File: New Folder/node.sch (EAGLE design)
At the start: 11 parts, among them IC1 TINY24/44/84-SSU

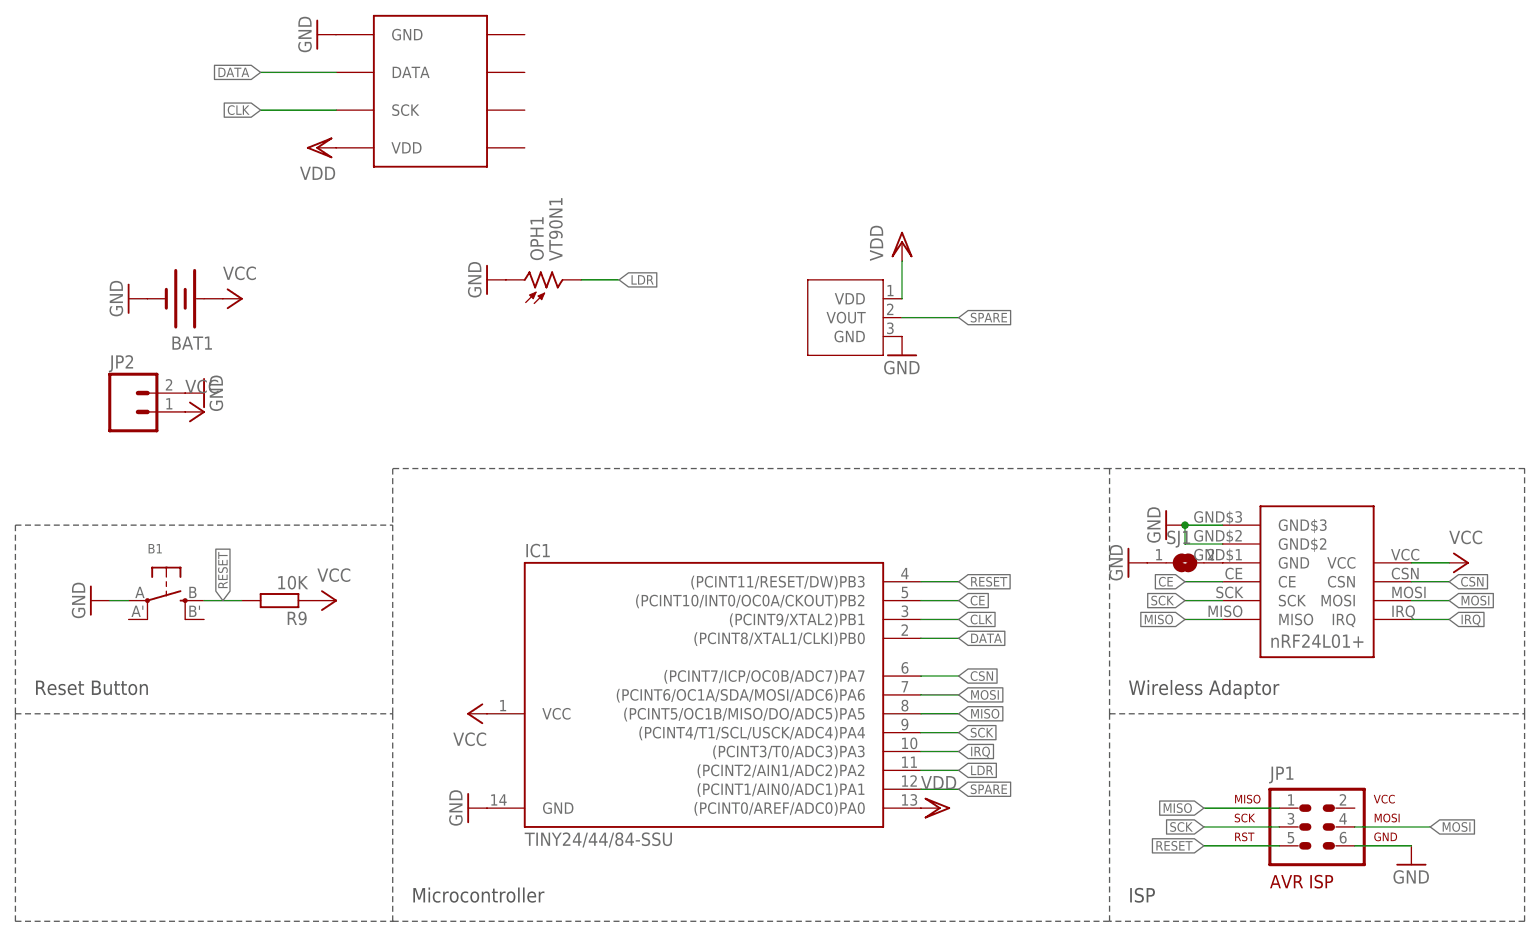
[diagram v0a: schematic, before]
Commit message: Added HA node v0.2, now with battery voltage monitoring
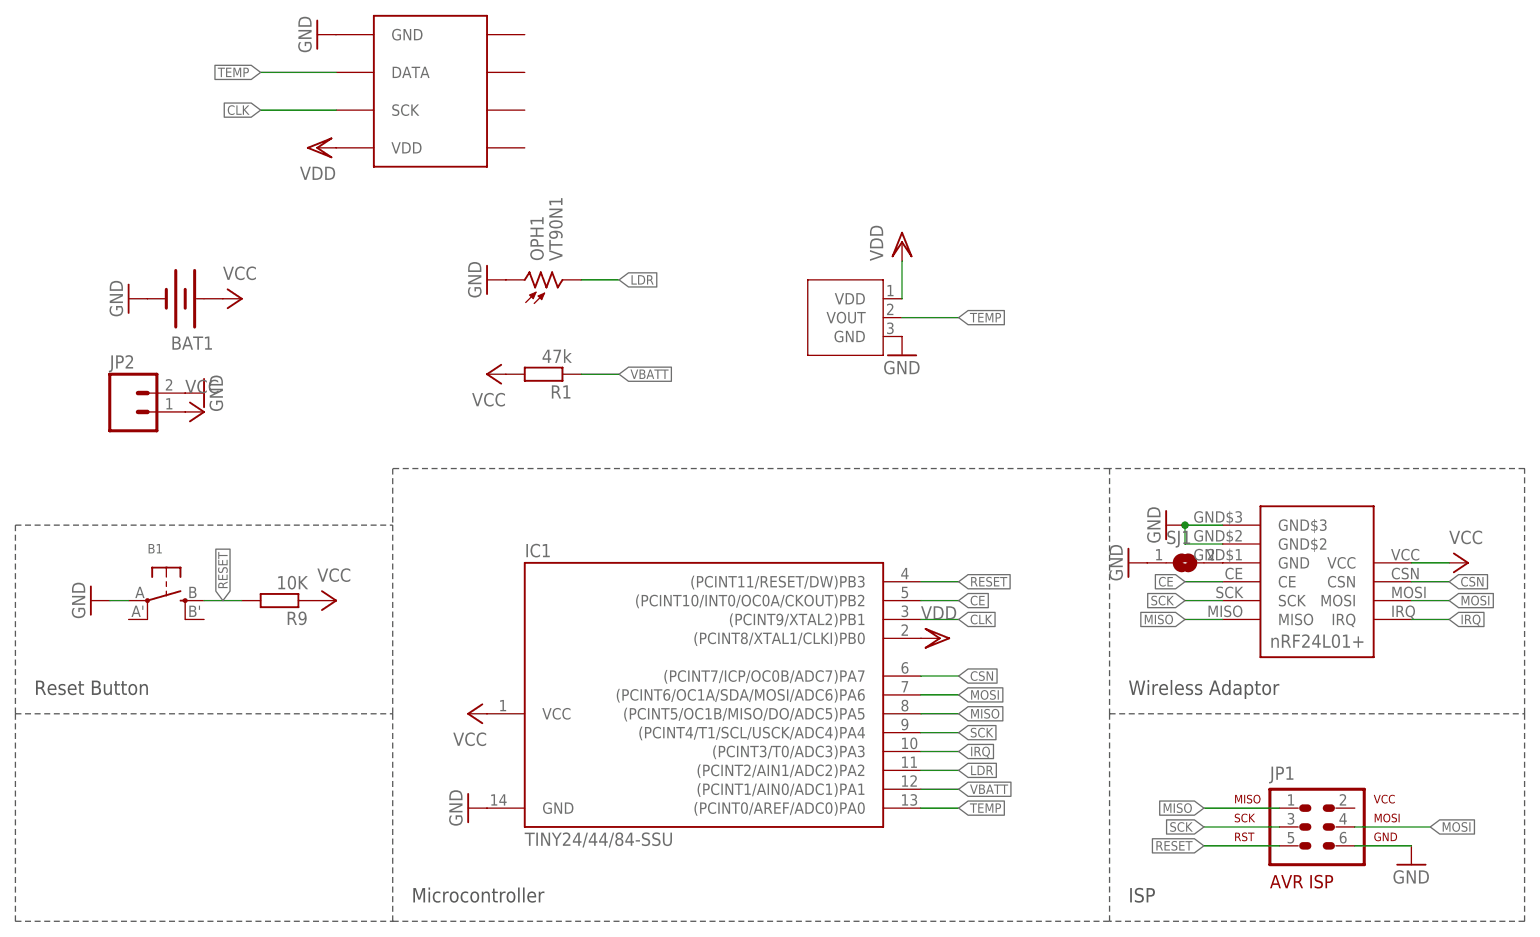
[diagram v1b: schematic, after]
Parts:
- added R1: 47k, rcl:R-EU_R0805
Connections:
- removed net DATA: IC1.(PCINT8/XTAL1/CLKI)PB0, SHT1.DATA
- removed net SPARE: IC1.(PCINT1/AIN0/ADC1)PA1, U$1.VOUT
- new net TEMP: IC1.(PCINT0/AREF/ADC0)PA0, SHT1.DATA, U$1.VOUT
- new net VBATT: IC1.(PCINT1/AIN0/ADC1)PA1, R1.1
- net VCC: now also R1.2
- net VDD: now also IC1.(PCINT8/XTAL1/CLKI)PB0; no longer IC1.(PCINT0/AREF/ADC0)PA0
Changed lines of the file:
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@@
 <grid distance="0.1" unitdist="inch" unit="inch" style="lines" multiple="1" display="no" altdistance="0.01" altunitdist="inch" altunit="inch"/>
 <layers>
-<layer number="1" name="Top" color="4" fill="1" visible="yes" active="no"/>
-<layer number="16" name="Bottom" color="1" fill="1" visible="yes" active="no"/>
-<layer number="17" name="Pads" color="2" fill="1" visible="yes" active="no"/>
-<layer number="18" name="Vias" color="2" fill="1" visible="yes" active="no"/>
-<layer number="19" name="Unrouted" color="6" fill="1" visible="yes" active="no"/>
-<layer number="20" name="Dimension" color="15" fill="1" visible="yes" active="no"/>
-<layer number="21" name="tPlace" color="7" fill="1" visible="yes" active="no"/>
-<layer number="22" name="bPlace" color="7" fill="1" visible="yes" active="no"/>
-<layer number="23" name="tOrigins" color="15" fill="1" visible="yes" active="no"/>
-<layer number="24" name="bOrigins" color="15" fill="1" visible="yes" active="no"/>
-<layer number="25" name="tNames" color="7" fill="1" visible="yes" active="no"/>
-<layer number="26" name="bNames" color="7" fill="1" visible="yes" active="no"/>
-<layer number="27" name="tValues" color="7" fill="1" visible="yes" active="no"/>
-<layer number="28" name="bValues" color="7" fill="1" visible="yes" active="no"/>
+<layer number="1" name="Top" color="4" fill="1" visible="no" active="no"/>
+<layer number="16" name="Bottom" color="1" fill="1" visible="no" active="no"/>
+<layer number="17" name="Pads" color="2" fill="1" visible="no" active="no"/>
+<layer number="18" name="Vias" color="2" fill="1" visible="no" active="no"/>
+<layer number="19" name="Unrouted" color="6" fill="1" visible="no" active="no"/>
+<layer number="20" name="Dimension" color="15" fill="1" visible="no" active="no"/>
+<layer number="21" name="tPlace" color="7" fill="1" visible="no" active="no"/>
+<layer number="22" name="bPlace" color="7" fill="1" visible="no" active="no"/>
+<layer number="23" name="tOrigins" color="15" fill="1" visible="no" active="no"/>
+<layer number="24" name="bOrigins" color="15" fill="1" visible="no" active="no"/>
+<layer number="25" name="tNames" color="7" fill="1" visible="no" active="no"/>
+<layer number="26" name="bNames" color="7" fill="1" visible="no" active="no"/>
+<layer number="27" name="tValues" color="7" fill="1" visible="no" active="no"/>
+<layer number="28" name="bValues" color="7" fill="1" visible="no" active="no"/>
 <layer number="29" name="tStop" color="7" fill="3" visible="no" active="no"/>
 <layer number="30" name="bStop" color="7" fill="6" visible="no" active="no"/>
@@
 <layer number="35" name="tGlue" color="7" fill="4" visible="no" active="no"/>
 <layer number="36" name="bGlue" color="7" fill="5" visible="no" active="no"/>
-<layer number="37" name="tTest" color="7" fill="1" visible="yes" active="no"/>
-<layer number="38" name="bTest" color="7" fill="1" visible="yes" active="no"/>
+<layer number="37" name="tTest" color="7" fill="1" visible="no" active="no"/>
+<layer number="38" name="bTest" color="7" fill="1" visible="no" active="no"/>
 <layer number="39" name="tKeepout" color="4" fill="11" visible="no" active="no"/>
 <layer number="40" name="bKeepout" color="1" fill="11" visible="no" active="no"/>
@@
 <layer number="44" name="Drills" color="7" fill="1" visible="no" active="no"/>
 <layer number="45" name="Holes" color="7" fill="1" visible="no" active="no"/>
-<layer number="46" name="Milling" color="3" fill="1" visible="yes" active="no"/>
-<layer number="47" name="Measures" color="7" fill="1" visible="yes" active="no"/>
-<layer number="48" name="Document" color="7" fill="1" visible="yes" active="no"/>
-<layer number="49" name="Reference" color="7" fill="1" visible="yes" active="no"/>
-<layer number="50" name="dxf" color="7" fill="1" visible="yes" active="no"/>
-<layer number="51" name="tDocu" color="7" fill="1" visible="yes" active="no"/>
-<layer number="52" name="bDocu" color="7" fill="1" visible="yes" active="no"/>
+<layer number="46" name="Milling" color="3" fill="1" visible="no" active="no"/>
+<layer number="47" name="Measures" color="7" fill="1" visible="no" active="no"/>
+<layer number="48" name="Document" color="7" fill="1" visible="no" active="no"/>
+<layer number="49" name="Reference" color="7" fill="1" visible="no" active="no"/>
+<layer number="50" name="dxf" color="7" fill="1" visible="no" active="no"/>
+<layer number="51" name="tDocu" color="7" fill="1" visible="no" active="no"/>
+<layer number="52" name="bDocu" color="7" fill="1" visible="no" active="no"/>
 <layer number="53" name="tGND_GNDA" color="7" fill="9" visible="no" active="no"/>
 <layer number="54" name="bGND_GNDA" color="1" fill="9" visible="no" active="no"/>
@@
 <part name="SHT1" library="sht11" deviceset="SHT11" device=""/>
 <part name="VDD1" library="supply1" deviceset="VDD" device=""/>
-<part name="VDD2" library="supply1" deviceset="VDD" device=""/>
 <part name="VDD3" library="supply1" deviceset="VDD" device=""/>
 <part name="GND9" library="supply1" deviceset="GND" device=""/>
+<part name="VDD2" library="supply1" deviceset="VDD" device=""/>
+<part name="R1" library="rcl" deviceset="R-EU_" device="R0805" value="47k"/>
+<part name="P+6" library="supply1" deviceset="VCC" device=""/>
 </parts>
 <sheets>
@@
 <instance part="SHT1" gate="SHT1X" x="0" y="93.98"/>
 <instance part="VDD1" gate="G$1" x="76.2" y="88.9"/>
-<instance part="VDD2" gate="G$1" x="81.28" y="12.7" rot="R270"/>
 <instance part="VDD3" gate="G$1" x="-2.54" y="101.6" rot="R90"/>
 <instance part="GND9" gate="1" x="-2.54" y="116.84" rot="R270"/>
+<instance part="VDD2" gate="G$1" x="81.28" y="35.56" rot="R270"/>
+<instance part="R1" gate="G$1" x="27.94" y="71.12" rot="R180"/>
+<instance part="P+6" gate="VCC" x="20.32" y="71.12" rot="R90"/>
 </instances>
 <busses>
@@
 <pinref part="P+2" gate="VCC" pin="VCC"/>
 <pinref part="BAT1" gate="G$1" pin="+"/>
+</segment>
+<segment>
+<pinref part="R1" gate="G$1" pin="2"/>
+<pinref part="P+6" gate="VCC" pin="VCC"/>
 </segment>
 </net>
@@
 </segment>
 </net>
-<net name="SPARE" class="0">
+<net name="VDD" class="0">
+<segment>
+<pinref part="U$1" gate="G$1" pin="VDD"/>
+<wire x1="76.2" y1="81.28" x2="76.2" y2="86.36" width="0.1524" layer="91"/>
+<pinref part="VDD1" gate="G$1" pin="VDD"/>
+</segment>
+<segment>
+<pinref part="SHT1" gate="SHT1X" pin="VDD"/>
+<pinref part="VDD3" gate="G$1" pin="VDD"/>
+</segment>
+<segment>
+<pinref part="IC1" gate="1" pin="(PCINT8/XTAL1/CLKI)PB0"/>
+<pinref part="VDD2" gate="G$1" pin="VDD"/>
+</segment>
+</net>
+<net name="CLK" class="0">
+<segment>
+<pinref part="SHT1" gate="SHT1X" pin="SCK"/>
+<wire x1="0" y1="106.68" x2="-10.16" y2="106.68" width="0.1524" layer="91"/>
+<label x="-10.16" y="106.68" size="1.27" layer="95" rot="R180" xref="yes"/>
+</segment>
+<segment>
+<wire x1="78.74" y1="38.1" x2="83.82" y2="38.1" width="0.1524" layer="91"/>
+<label x="83.82" y="38.1" size="1.27" layer="95" xref="yes"/>
+<pinref part="IC1" gate="1" pin="(PCINT9/XTAL2)PB1"/>
+</segment>
+</net>
+<net name="TEMP" class="0">
+<segment>
+<pinref part="IC1" gate="1" pin="(PCINT0/AREF/ADC0)PA0"/>
+<wire x1="78.74" y1="12.7" x2="83.82" y2="12.7" width="0.1524" layer="91"/>
+<label x="83.82" y="12.7" size="1.27" layer="95" xref="yes"/>
+</segment>
+<segment>
+<pinref part="U$1" gate="G$1" pin="VOUT"/>
+<wire x1="76.2" y1="78.74" x2="83.82" y2="78.74" width="0.1524" layer="91"/>
+<label x="83.82" y="78.74" size="1.27" layer="95" xref="yes"/>
+</segment>
+<segment>
+<pinref part="SHT1" gate="SHT1X" pin="DATA"/>
+<wire x1="0" y1="111.76" x2="-10.16" y2="111.76" width="0.1524" layer="91"/>
+<label x="-10.16" y="111.76" size="1.27" layer="95" rot="R180" xref="yes"/>
+</segment>
+</net>
+<net name="VBATT" class="0">
 <segment>
 <wire x1="78.74" y1="15.24" x2="83.82" y2="15.24" width="0.1524" layer="91"/>
@@
 </segment>
 <segment>
-<pinref part="U$1" gate="G$1" pin="VOUT"/>
-<wire x1="76.2" y1="78.74" x2="83.82" y2="78.74" width="0.1524" layer="91"/>
-<label x="83.82" y="78.74" size="1.27" layer="95" xref="yes"/>
-</segment>
-</net>
-<net name="VDD" class="0">
-<segment>
-<pinref part="U$1" gate="G$1" pin="VDD"/>
-<wire x1="76.2" y1="81.28" x2="76.2" y2="86.36" width="0.1524" layer="91"/>
-<pinref part="VDD1" gate="G$1" pin="VDD"/>
-</segment>
-<segment>
-<pinref part="IC1" gate="1" pin="(PCINT0/AREF/ADC0)PA0"/>
-<pinref part="VDD2" gate="G$1" pin="VDD"/>
-</segment>
-<segment>
-<pinref part="SHT1" gate="SHT1X" pin="VDD"/>
-<pinref part="VDD3" gate="G$1" pin="VDD"/>
-</segment>
-</net>
-<net name="DATA" class="0">
-<segment>
-<pinref part="SHT1" gate="SHT1X" pin="DATA"/>
-<wire x1="0" y1="111.76" x2="-10.16" y2="111.76" width="0.1524" layer="91"/>
-<label x="-10.16" y="111.76" size="1.27" layer="95" rot="R180" xref="yes"/>
-</segment>
-<segment>
-<wire x1="78.74" y1="35.56" x2="83.82" y2="35.56" width="0.1524" layer="91"/>
-<label x="83.82" y="35.56" size="1.27" layer="95" xref="yes"/>
-<pinref part="IC1" gate="1" pin="(PCINT8/XTAL1/CLKI)PB0"/>
-</segment>
-</net>
-<net name="CLK" class="0">
-<segment>
-<pinref part="SHT1" gate="SHT1X" pin="SCK"/>
-<wire x1="0" y1="106.68" x2="-10.16" y2="106.68" width="0.1524" layer="91"/>
-<label x="-10.16" y="106.68" size="1.27" layer="95" rot="R180" xref="yes"/>
-</segment>
-<segment>
-<wire x1="78.74" y1="38.1" x2="83.82" y2="38.1" width="0.1524" layer="91"/>
-<label x="83.82" y="38.1" size="1.27" layer="95" xref="yes"/>
-<pinref part="IC1" gate="1" pin="(PCINT9/XTAL2)PB1"/>
-</segment>
-</net>
+<pinref part="R1" gate="G$1" pin="1"/>
+<wire x1="33.02" y1="71.12" x2="38.1" y2="71.12" width="0.1524" layer="91"/>
+<label x="38.1" y="71.12" size="1.27" layer="95" xref="yes"/>
+</segment>
+</net>
